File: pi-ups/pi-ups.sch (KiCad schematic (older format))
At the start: 31 parts, among them J1 , Q1 IRLML2244, Q2 IRLML2244, Q3 IRLML2244, Q4 IRLML2244, U1 BMS_1S, U2 DC-DC, U3 BMS_1S, U4 FTDI232, U5 Arduino_Pro_Mini

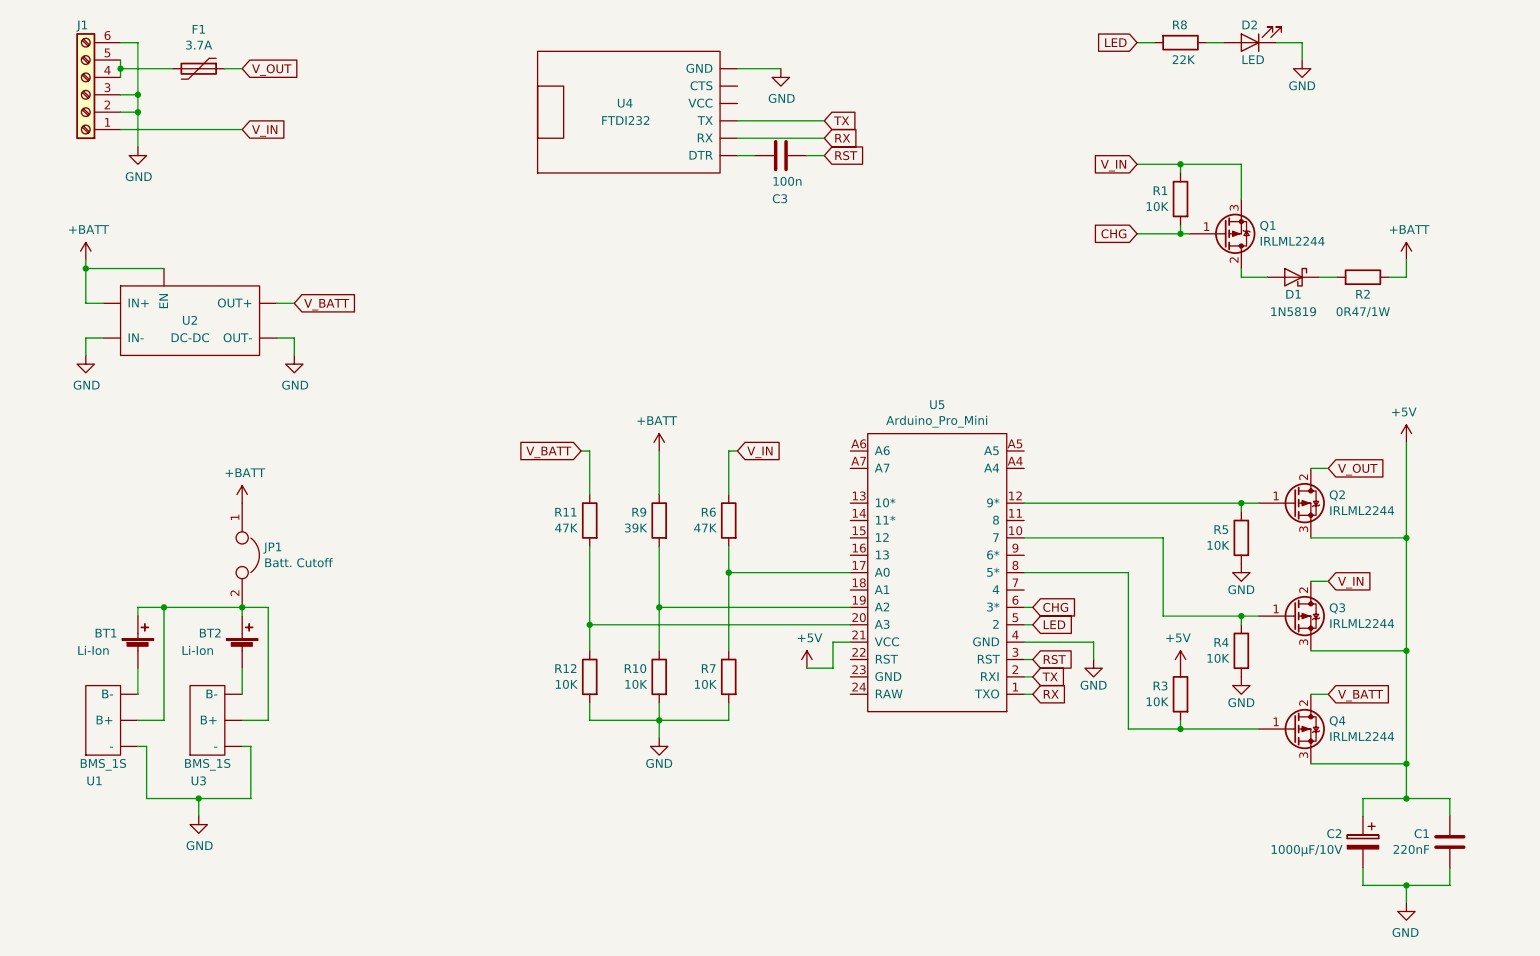
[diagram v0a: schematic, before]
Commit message: pi-ups: more tidy
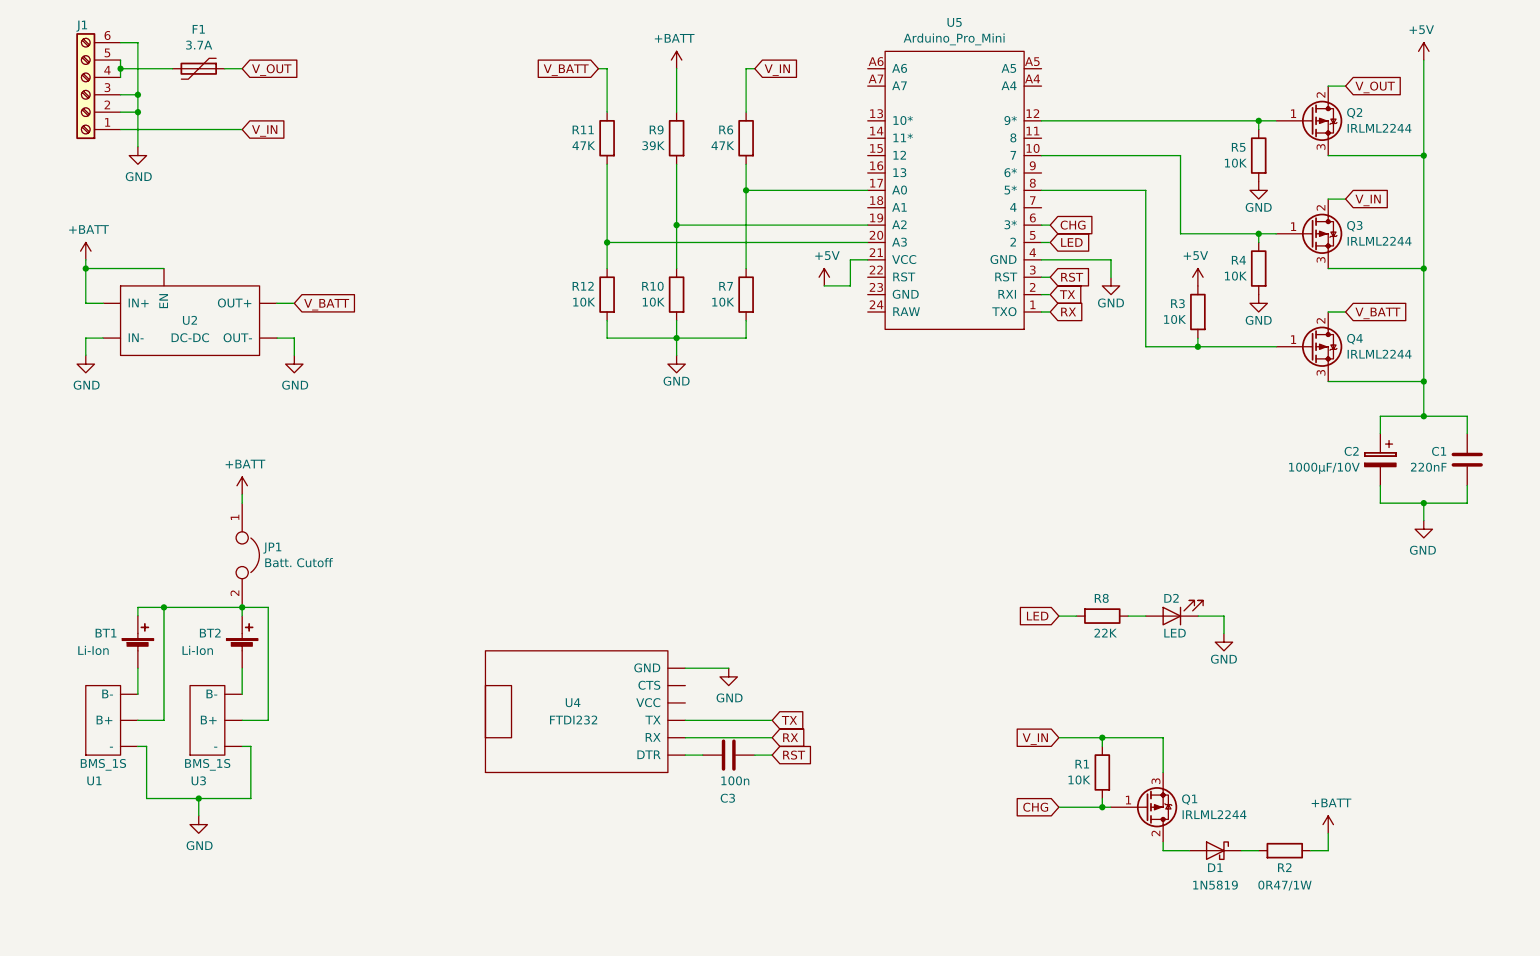
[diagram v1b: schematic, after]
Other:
- moved on the sheet: C1, C2, C3, D1, D2, Q1, Q2, Q3, Q4, R1, R10, R11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

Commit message: pi-ups: annotate
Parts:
- renumbered C3 to C1, C1 to C3, D2 to D1, D1 to D2, R11 to R1, R5 to R10, R4 to R11, R2 to R12, R12 to R2, R9 to R3, R10 to R4, R6 to R5, R7 to R6, R8 to R7, R1 to R8, R3 to R9
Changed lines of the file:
@@
 $EndComp
 $Comp
-L power:GND #PWR014
+L power:GND #PWR09
 U 1 1 5CDDD224
 P 5700 4850
-F 0 "#PWR014" H 5700 4600 50  0001 C CNN
+F 0 "#PWR09" H 5700 4600 50  0001 C CNN
 F 1 "GND" H 5705 4677 50  0000 C CNN
 F 2 "" H 5700 4850 50  0001 C CNN
@@
 $EndComp
 $Comp
-L Device:C C3
+L Device:C C1
 U 1 1 5CDDD4BF
 P 5700 5350
-F 0 "C3" V 5950 5400 50  0000 R CNN
+F 0 "C1" V 5950 5400 50  0000 R CNN
 F 1 "100n" V 5850 5400 50  0000 R CNN
 F 2 "" H 5738 5200 50  0001 C CNN
@@
 $EndComp
 $Comp
-L power:+5V #PWR08
+L power:+5V #PWR017
 U 1 1 5CDF6DD4
 P 9700 1350
-F 0 "#PWR08" H 9700 1200 50  0001 C CNN
+F 0 "#PWR017" H 9700 1200 50  0001 C CNN
 F 1 "+5V" H 9715 1523 50  0000 C CNN
 F 2 "" H 9700 1350 50  0001 C CNN
@@
 	2800 1400 2900 1400
 $Comp
-L power:+5V #PWR015
+L power:+5V #PWR010
 U 1 1 5CE042BB
 P 6250 2650
-F 0 "#PWR015" H 6250 2500 50  0001 C CNN
+F 0 "#PWR010" H 6250 2500 50  0001 C CNN
 F 1 "+5V" H 6265 2823 50  0000 C CNN
 F 2 "" H 6250 2650 50  0001 C CNN
@@
 $EndComp
 $Comp
-L power:GND #PWR013
+L power:GND #PWR011
 U 1 1 5CE04E5A
 P 7900 2600
-F 0 "#PWR013" H 7900 2350 50  0001 C CNN
+F 0 "#PWR011" H 7900 2350 50  0001 C CNN
 F 1 "GND" H 7900 2450 50  0000 C CNN
 F 2 "" H 7900 2600 50  0001 C CNN
@@
 $EndComp
 $Comp
-L Device:C C1
+L Device:C C3
 U 1 1 5CE05C0B
 P 9950 3650
-F 0 "C1" H 9835 3696 50  0000 R CNN
+F 0 "C3" H 9835 3696 50  0000 R CNN
 F 1 "220nF" H 9835 3605 50  0000 R CNN
 F 2 "" H 9988 3500 50  0001 C CNN
@@
 	9700 3200 9150 3200
 $Comp
-L power:GND #PWR09
+L power:GND #PWR018
 U 1 1 5CE0B0C6
 P 9700 4000
-F 0 "#PWR09" H 9700 3750 50  0001 C CNN
+F 0 "#PWR018" H 9700 3750 50  0001 C CNN
 F 1 "GND" H 9705 3827 50  0000 C CNN
 F 2 "" H 9700 4000 50  0001 C CNN
@@
 	9250 1500 9150 1500
 $Comp
-L Device:R R3
+L Device:R R9
 U 1 1 5CE70A4E
 P 8400 2800
-F 0 "R3" H 8470 2846 50  0000 L CNN
+F 0 "R9" H 8470 2846 50  0000 L CNN
 F 1 "10K" H 8470 2755 50  0000 L CNN
 F 2 "" V 8330 2800 50  0001 C CNN
@@
 $EndComp
 $Comp
-L power:+5V #PWR010
+L power:+5V #PWR012
 U 1 1 5CE7427A
 P 8400 2650
-F 0 "#PWR010" H 8400 2500 50  0001 C CNN
+F 0 "#PWR012" H 8400 2500 50  0001 C CNN
 F 1 "+5V" H 8415 2823 50  0000 C CNN
 F 2 "" H 8400 2650 50  0001 C CNN
@@
 $EndComp
 $Comp
-L Device:R R4
+L Device:R R11
 U 1 1 5CE743B7
 P 8750 2550
-F 0 "R4" H 8820 2596 50  0000 L CNN
+F 0 "R11" H 8820 2596 50  0000 L CNN
 F 1 "10K" H 8820 2505 50  0000 L CNN
 F 2 "" V 8680 2550 50  0001 C CNN
@@
 $EndComp
 $Comp
-L power:GND #PWR011
+L power:GND #PWR015
 U 1 1 5CE74402
 P 8750 2700
-F 0 "#PWR011" H 8750 2450 50  0001 C CNN
+F 0 "#PWR015" H 8750 2450 50  0001 C CNN
 F 1 "GND" H 8750 2550 50  0000 C CNN
 F 2 "" H 8750 2700 50  0001 C CNN
@@
 	8750 2350 8300 2350
 $Comp
-L Device:R R5
+L Device:R R10
 U 1 1 5CE76087
 P 8750 1900
-F 0 "R5" H 8820 1946 50  0000 L CNN
+F 0 "R10" H 8820 1946 50  0000 L CNN
 F 1 "10K" H 8820 1855 50  0000 L CNN
 F 2 "" V 8680 1900 50  0001 C CNN
@@
 $EndComp
 $Comp
-L power:GND #PWR012
+L power:GND #PWR014
 U 1 1 5CE760C6
 P 8750 2050
-F 0 "#PWR012" H 8750 1800 50  0001 C CNN
+F 0 "#PWR014" H 8750 1800 50  0001 C CNN
 F 1 "GND" H 8750 1900 50  0000 C CNN
 F 2 "" H 8750 2050 50  0001 C CNN
@@
 $EndComp
 $Comp
-L Device:R R7
+L Device:R R6
 U 1 1 5CE7C356
 P 5800 2700
-F 0 "R7" H 5870 2746 50  0000 L CNN
+F 0 "R6" H 5870 2746 50  0000 L CNN
 F 1 "10K" H 5870 2655 50  0000 L CNN
 F 2 "" V 5730 2700 50  0001 C CNN
@@
 $EndComp
 $Comp
-L Device:R R10
+L Device:R R4
 U 1 1 5CE7E21F
 P 5400 2700
-F 0 "R10" H 5470 2746 50  0000 L CNN
+F 0 "R4" H 5470 2746 50  0000 L CNN
 F 1 "10K" H 5470 2655 50  0000 L CNN
 F 2 "" V 5330 2700 50  0001 C CNN
@@
 $EndComp
 $Comp
-L Device:R R12
+L Device:R R2
 U 1 1 5CE7E25D
 P 5000 2700
-F 0 "R12" H 5070 2746 50  0000 L CNN
+F 0 "R2" H 5070 2746 50  0000 L CNN
 F 1 "10K" H 5070 2655 50  0000 L CNN
 F 2 "" V 4930 2700 50  0001 C CNN
@@
 	5000 2950 5000 2850
 $Comp
-L power:GND #PWR018
+L power:GND #PWR08
 U 1 1 5CE8025B
 P 5400 3050
-F 0 "#PWR018" H 5400 2800 50  0001 C CNN
+F 0 "#PWR08" H 5400 2800 50  0001 C CNN
 F 1 "GND" H 5400 2900 50  0000 C CNN
 F 2 "" H 5400 3050 50  0001 C CNN
@@
 	5400 2850 5400 2950
 $Comp
-L Device:R R6
+L Device:R R5
 U 1 1 5CE843C8
 P 5800 1800
-F 0 "R6" H 5870 1846 50  0000 L CNN
+F 0 "R5" H 5870 1846 50  0000 L CNN
 F 1 "47K" H 5870 1755 50  0000 L CNN
 F 2 "" V 5730 1800 50  0001 C CNN
@@
 $EndComp
 $Comp
-L Device:R R9
+L Device:R R3
 U 1 1 5CE8442D
 P 5400 1800
-F 0 "R9" H 5470 1846 50  0000 L CNN
+F 0 "R3" H 5470 1846 50  0000 L CNN
 F 1 "39K" H 5470 1755 50  0000 L CNN
 F 2 "" V 5330 1800 50  0001 C CNN
@@
 $EndComp
 $Comp
-L Device:R R11
+L Device:R R1
 U 1 1 5CE84472
 P 5000 1800
-F 0 "R11" H 5070 1846 50  0000 L CNN
+F 0 "R1" H 5070 1846 50  0000 L CNN
 F 1 "47K" H 5070 1755 50  0000 L CNN
 F 2 "" V 4930 1800 50  0001 C CNN
@@
 	5800 1400 5800 1650
 $Comp
-L power:+BATT #PWR017
+L power:+BATT #PWR07
 U 1 1 5CEA4FDB
 P 5400 1400
-F 0 "#PWR017" H 5400 1250 50  0001 C CNN
+F 0 "#PWR07" H 5400 1250 50  0001 C CNN
 F 1 "+BATT" H 5415 1573 50  0000 C CNN
 F 2 "" H 5400 1400 50  0001 C CNN
@@
 LED
 $Comp
-L Device:R R8
+L Device:R R7
 U 1 1 5CED4311
 P 7850 4550
-F 0 "R8" V 7750 4500 50  0000 L CNN
+F 0 "R7" V 7750 4500 50  0000 L CNN
 F 1 "22K" V 7950 4500 50  0000 L CNN
 F 2 "" V 7780 4550 50  0001 C CNN
@@
 $EndComp
 $Comp
-L Device:LED D2
+L Device:LED D1
 U 1 1 5CED4485
 P 8250 4550
-F 0 "D2" H 8300 4450 50  0000 R CNN
+F 0 "D1" H 8300 4450 50  0000 R CNN
 F 1 "LED" H 8300 4650 50  0000 R CNN
 F 2 "" H 8250 4550 50  0001 C CNN
@@
 $EndComp
 $Comp
-L power:GND #PWR016
+L power:GND #PWR013
 U 1 1 5CED458D
 P 8550 4650
-F 0 "#PWR016" H 8550 4400 50  0001 C CNN
+F 0 "#PWR013" H 8550 4400 50  0001 C CNN
 F 1 "GND" H 8550 4500 50  0000 C CNN
 F 2 "" H 8550 4650 50  0001 C CNN
@@
 $EndComp
 $Comp
-L Diode:1N5819 D1
+L Diode:1N5819 D2
 U 1 1 5CEFC83C
 P 8500 5900
-F 0 "D1" H 8500 5800 50  0000 C CNN
+F 0 "D2" H 8500 5800 50  0000 C CNN
 F 1 "1N5819" H 8500 5700 50  0000 C CNN
 F 2 "Diode_THT:D_DO-41_SOD81_P10.16mm_Horizontal" H 8500 5725 50  0001 C CNN
@@
 $EndComp
 $Comp
-L Device:R R2
+L Device:R R12
 U 1 1 5CEFC924
 P 8900 5900
-F 0 "R2" V 8800 5900 50  0000 C CNN
+F 0 "R12" V 8800 5900 50  0000 C CNN
 F 1 "0R47/1W" V 8700 5900 50  0000 C CNN
 F 2 "" V 8830 5900 50  0001 C CNN
@@
 $EndComp
 $Comp
-L Device:R R1
+L Device:R R8
 U 1 1 5CF0264E
 P 7850 5450
-F 0 "R1" H 7920 5496 50  0000 L CNN
+F 0 "R8" H 7920 5496 50  0000 L CNN
 F 1 "10K" H 7920 5405 50  0000 L CNN
 F 2 "" V 7780 5450 50  0001 C CNN
@@
 	8200 5900 8350 5900
 $Comp
-L power:+BATT #PWR07
+L power:+BATT #PWR016
 U 1 1 5CF56082
 P 9150 5800
-F 0 "#PWR07" H 9150 5650 50  0001 C CNN
+F 0 "#PWR016" H 9150 5650 50  0001 C CNN
 F 1 "+BATT" H 9165 5973 50  0000 C CNN
 F 2 "" H 9150 5800 50  0001 C CNN

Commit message: pi-ups: correct input/output labels
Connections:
- net V_BATT: now also JP1.1, R12.1, R3.1; no longer Q4.2 (D), R1.1
- removed net +BATT: JP1.1, R12.1, R3.1, U2.~ (OUT-)
- new net V_UPS: Q4.2 (D), R1.1, U2.~ (OUT-)
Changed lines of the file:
@@
 Text GLabel 5950 5250 2    50   Input ~ 0
 RX
-Text GLabel 5950 5150 2    50   Input ~ 0
+Text GLabel 5950 5150 2    50   Output ~ 0
 TX
 Wire Wire Line
@@
 Wire Wire Line
 	5550 5350 5450 5350
-Text GLabel 5950 5350 2    50   Input ~ 0
+Text GLabel 5950 5350 2    50   Output ~ 0
 RST
 Wire Wire Line
@@
 Text GLabel 7550 2700 2    50   Input ~ 0
 TX
-Text GLabel 7550 2800 2    50   Input ~ 0
+Text GLabel 7550 2800 2    50   Output ~ 0
 RX
 Wire Wire Line
@@
 	1    0    0    -1
 $EndComp
-Text GLabel 2900 1750 2    50   Input ~ 0
+Text GLabel 2900 1750 2    50   Output ~ 0
 V_IN
 Wire Wire Line
@@
 Wire Wire Line
 	5450 4850 5700 4850
-Text GLabel 3200 2750 2    50   Input ~ 0
-V_BATT
+Text GLabel 3200 2750 2    50   Output ~ 0
+V_UPS
 Wire Wire Line
 	2450 4500 2900 4500
@@
 	8850 2350 8750 2350
 Text GLabel 9250 2800 2    50   Input ~ 0
-V_BATT
+V_UPS
 Wire Wire Line
 	9250 2800 9150 2800
@@
 	1    0    0    -1
 $EndComp
-$Comp
-L power:+BATT #PWR05
-U 1 1 5CE2F6C4
-P 2900 3850
-F 0 "#PWR05" H 2900 3700 50  0001 C CNN
-F 1 "+BATT" H 2915 4023 50  0000 C CNN
-F 2 "" H 2900 3850 50  0001 C CNN
-F 3 "" H 2900 3850 50  0001 C CNN
-	1    2900 3850
-	1    0    0    -1
-$EndComp
 Wire Wire Line
 	3100 2750 3200 2750
@@
 	3200 2950 3200 3050
 $Comp
-L power:+BATT #PWR01
-U 1 1 5CE436AA
-P 2000 2500
-F 0 "#PWR01" H 2000 2350 50  0001 C CNN
-F 1 "+BATT" H 2015 2673 50  0000 C CNN
-F 2 "" H 2000 2500 50  0001 C CNN
-F 3 "" H 2000 2500 50  0001 C CNN
-	1    2000 2500
-	1    0    0    -1
-$EndComp
-$Comp
 L power:GND #PWR02
 U 1 1 5CE49B9B
@@
 Wire Wire Line
 	2000 2950 2100 2950
-Wire Wire Line
-	2100 2750 2000 2750
-Wire Wire Line
-	2000 2750 2000 2550
-Wire Wire Line
-	2000 2550 2450 2550
-Text GLabel 9250 1500 2    50   Input ~ 0
+Text GLabel 9250 1500 2    50   Output ~ 0
 V_OUT
 Wire Wire Line
@@
 	-1   0    0    -1
 $EndComp
-Text GLabel 5850 1400 2    50   Input ~ 0
+Text GLabel 5750 1400 0    50   Input ~ 0
 V_IN
 Wire Wire Line
-	5850 1400 5800 1400
+	5750 1400 5800 1400
 Wire Wire Line
 	5800 1400 5800 1650
-$Comp
-L power:+BATT #PWR07
-U 1 1 5CEA4FDB
-P 5400 1400
-F 0 "#PWR07" H 5400 1250 50  0001 C CNN
-F 1 "+BATT" H 5415 1573 50  0000 C CNN
-F 2 "" H 5400 1400 50  0001 C CNN
-F 3 "" H 5400 1400 50  0001 C CNN
-	1    5400 1400
-	-1   0    0    -1
-$EndComp
-Wire Wire Line
-	5400 1650 5400 1400
 Text GLabel 4950 1400 0    50   Input ~ 0
-V_BATT
+V_UPS
 Wire Wire Line
 	5000 1650 5000 1400
 Wire Wire Line
 	5000 1400 4950 1400
-Text GLabel 7550 2400 2    50   Input ~ 0
+Text GLabel 7550 2400 2    50   Output ~ 0
 LED
 Wire Wire Line
@@
 	1    0    0    -1
 $EndComp
-Text GLabel 7550 2300 2    50   Input ~ 0
+Text GLabel 7550 2300 2    50   Output ~ 0
 CHG
 Wire Wire Line
@@
 	8200 5250 8200 5450
 Wire Wire Line
-	2000 2550 2000 2500
-Connection ~ 2000 2550
-Wire Wire Line
 	8650 5900 8750 5900
 Wire Wire Line
@@
 Wire Wire Line
 	8200 5900 8350 5900
-$Comp
-L power:+BATT #PWR016
-U 1 1 5CF56082
-P 9150 5800
-F 0 "#PWR016" H 9150 5650 50  0001 C CNN
-F 1 "+BATT" H 9165 5973 50  0000 C CNN
-F 2 "" H 9150 5800 50  0001 C CNN
-F 3 "" H 9150 5800 50  0001 C CNN
-	1    9150 5800
-	1    0    0    -1
-$EndComp
-Wire Wire Line
-	9150 5800 9150 5900
 Wire Wire Line
 	9150 5900 9050 5900
@@
 Wire Wire Line
 	2900 3900 2900 3850
+Text GLabel 3000 3850 2    50   BiDi ~ 0
+V_BATT
+Wire Wire Line
+	2900 3850 3000 3850
+Text GLabel 2000 2750 0    50   Input ~ 0
+V_BATT
+Wire Wire Line
+	2450 2550 2100 2550
+Wire Wire Line
+	2100 2550 2100 2750
+Connection ~ 2100 2750
+Wire Wire Line
+	2100 2750 2000 2750
+Text GLabel 9150 5900 2    50   Output ~ 0
+V_BATT
+Text GLabel 5350 1200 0    50   Input ~ 0
+V_BATT
+Wire Wire Line
+	5350 1200 5400 1200
+Wire Wire Line
+	5400 1200 5400 1650
 $EndSCHEMATC

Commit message: pi-ups: separate power channels
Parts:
- removed F1: 3.7A, symbol Device:Polyfuse
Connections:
- net V_OUT is gone; now on net V_RPI: Q2.2 (D)
- net +5V: now also J1.4 (Pin_4)
- net V_RPI: now reaches J1.5 (Pin_5)
- net V_RPI: no longer J1.4 (Pin_4)
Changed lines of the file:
@@
 	1    0    0    -1
 $EndComp
-Text GLabel 2900 1750 2    50   Output ~ 0
+Text GLabel 2550 1750 2    50   Output ~ 0
 V_IN
 Wire Wire Line
@@
 	2300 1250 2300 1550
 Connection ~ 2300 1550
-Text GLabel 2900 1400 2    50   Input ~ 0
-V_OUT
-Wire Wire Line
-	2200 1750 2900 1750
+Text GLabel 2550 1350 2    50   Input ~ 0
+V_RPI
+Wire Wire Line
+	2200 1750 2550 1750
 $Comp
 L Device:Battery_Cell BT1
@@
 	-1   0    0    -1
 $EndComp
-$Comp
-L Device:Polyfuse F1
-U 1 1 5CDF8A9B
-P 2650 1400
-F 0 "F1" V 2425 1400 50  0000 C CNN
-F 1 "3.7A" V 2516 1400 50  0000 C CNN
-F 2 "" H 2700 1200 50  0001 L CNN
-F 3 "~" H 2650 1400 50  0001 C CNN
-	1    2650 1400
-	0    1    1    0
-$EndComp
-Wire Wire Line
-	2200 1350 2200 1400
-Wire Wire Line
-	2200 1400 2500 1400
-Connection ~ 2200 1400
-Wire Wire Line
-	2200 1400 2200 1450
-Wire Wire Line
-	2800 1400 2900 1400
 $Comp
 L power:+5V #PWR010
@@
 	2000 2950 2100 2950
 Text GLabel 9250 1500 2    50   Output ~ 0
-V_OUT
+V_RPI
 Wire Wire Line
 	9250 1500 9150 1500
@@
 Wire Wire Line
 	5400 1200 5400 1650
+Text GLabel 9900 3200 2    50   Output ~ 0
+V_HDD
+Text GLabel 2550 1450 2    50   Input ~ 0
+V_HDD
+Wire Wire Line
+	9700 3200 9900 3200
+Wire Wire Line
+	2200 1350 2550 1350
+Wire Wire Line
+	2200 1450 2550 1450
 $EndSCHEMATC
